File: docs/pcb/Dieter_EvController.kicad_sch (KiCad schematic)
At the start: 38 parts, among them IC1 ADS1118QDGSRQ1, J1 HVDC_POS, J2 HVDC_NEG, J6 lock_motor, J7 inputs, J8 relay board, J9 PLC_modem, Q1 set state c, U6 ISOW7741

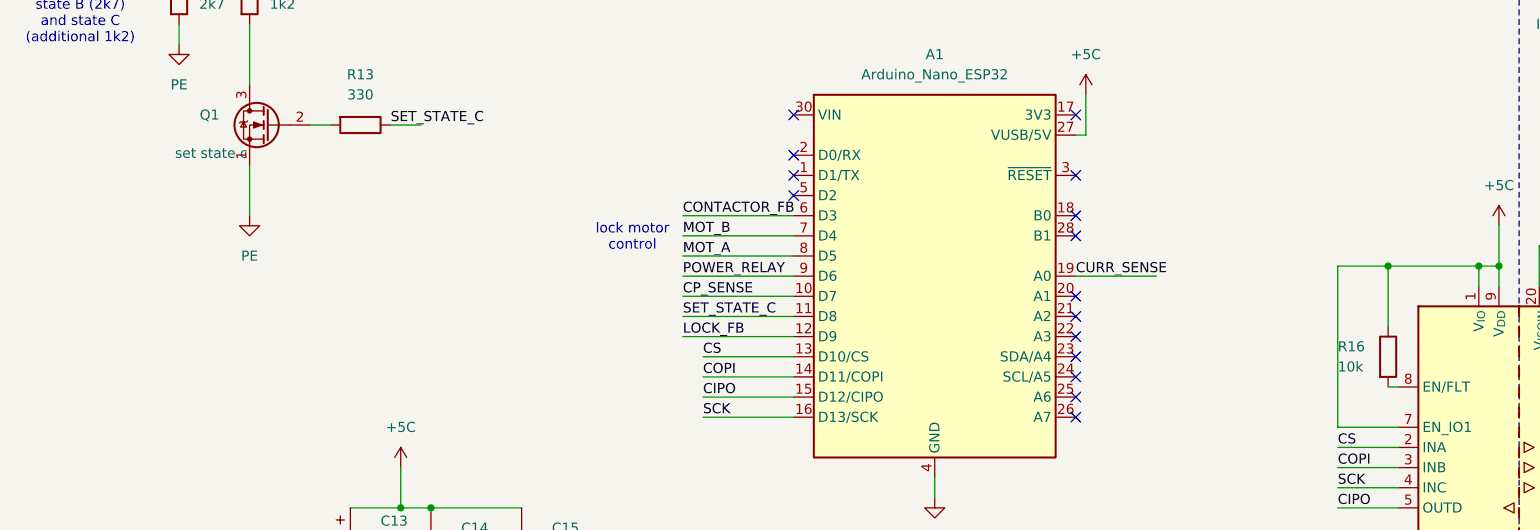
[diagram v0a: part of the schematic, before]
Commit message: documentation: add mounting + corrected pcb source files; BOM
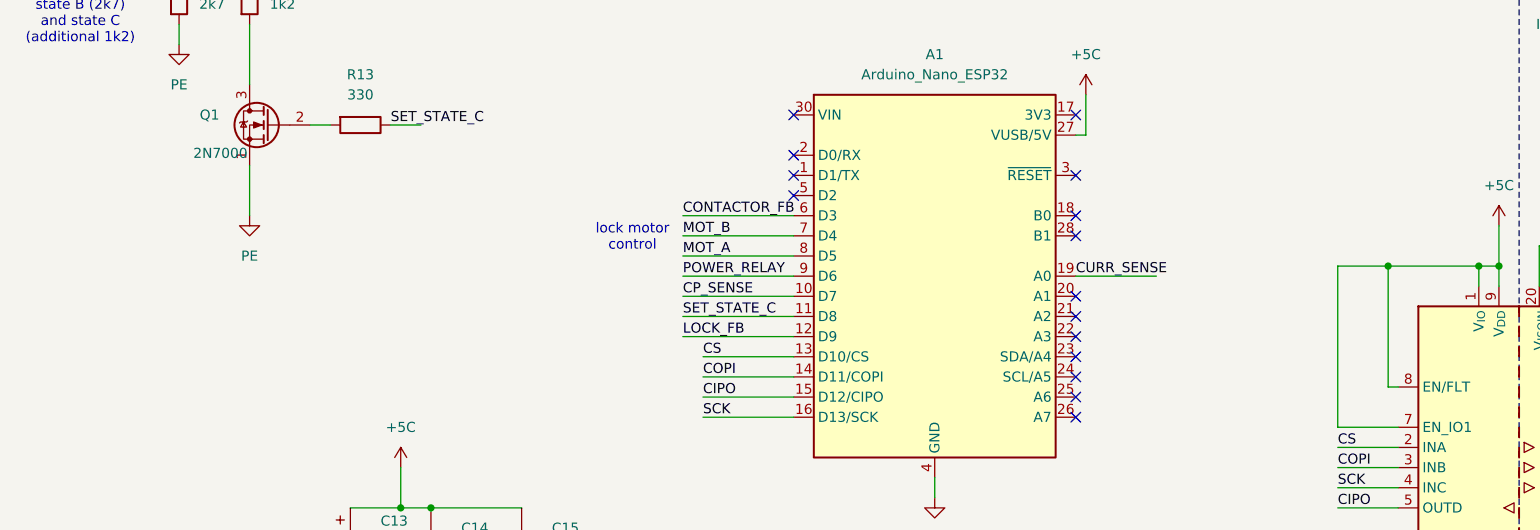
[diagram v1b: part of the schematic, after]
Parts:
- removed R16: 10k, Resistor_THT:R_Axial_DIN0204_L3.6mm_D1.6mm_P7.62mm_Horizontal, symbol Device:R
- Q1: value set state c -> 2N7000
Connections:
- net +5C: now also U6.8 (EN/FLT)
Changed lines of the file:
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@@
 	(wire
 		(pts
-			(xy 191.77 106.68) (xy 191.77 114.3)
+			(xy 191.77 106.68) (xy 191.77 121.92)
 		)
 		(stroke
@@
 			)
 		)
-		(property "Value" "set state c"
+		(property "Value" "2N7000"
 			(at 48.006 92.456 0)
 			(show_name no)
@@
 					(unit 1)
 				)
-			)
-		)
-	)
-	(symbol
-		(lib_id "Device:R")
-		(at 191.77 118.11 0)
-		(unit 1)
-		(body_style 1)
-		(exclude_from_sim no)
-		(in_bom yes)
-		(on_board yes)
-		(in_pos_files yes)
-		(dnp no)
-		(property "Reference" "R16"
-			(at 185.42 116.8399 0)
-			(show_name no)
-			(do_not_autoplace no)
-			(effects
-				(font
-					(size 1.27 1.27)
-				)
-				(justify left)
-			)
-		)
-		(property "Value" "10k"
-			(at 185.42 119.3799 0)
-			(show_name no)
-			(do_not_autoplace no)
-			(effects
-				(font
-					(size 1.27 1.27)
-				)
-				(justify left)
-			)
-		)
-		(property "Footprint" "Resistor_THT:R_Axial_DIN0204_L3.6mm_D1.6mm_P7.62mm_Horizontal"
-			(at 189.992 118.11 90)
-			(hide yes)
-			(show_name no)
-			(do_not_autoplace no)
-			(effects
-				(font
-					(size 1.27 1.27)
-				)
-			)
-		)
-		(property "Datasheet" ""
-			(at 191.77 118.11 0)
-			(hide yes)
-			(show_name no)
-			(do_not_autoplace no)
-			(effects
-				(font
-					(size 1.27 1.27)
-				)
-			)
-		)
-		(property "Description" "Resistor"
-			(at 191.77 118.11 0)
-			(hide yes)
-			(show_name no)
-			(do_not_autoplace no)
-			(effects
-				(font
-					(size 1.27 1.27)
-				)
-			)
-		)
-		(pin "2"
-		)
-		(pin "1"
-		)
-		(instances
-			(project "Dieter_EvController"
-				(path "/6da216d1-fac2-4060-89d5-7e116092ddcb"
-					(reference "R16")
-					(unit 1)
-				)
